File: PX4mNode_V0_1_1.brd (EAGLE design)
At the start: 48.6 x 34.9 mm, 140 parts, among them J201 DF13C-6P-1.25V, J202 DF13C-6P-1.25V, J203 DF13C-6P-1.25V, J301 DF13C-4P-1.25V, J401 DF13C-7P-1.25V, J402 DF13-4P-1.25V, J403 DF13C-4P-1.25V, J404 DF13C-4P-1.25V, J405 DF13C-4P-1.25V, J801 DF13C-3P-1.25V, M3_MOUNT1101 MOUNT-HOLE3.1MM, M3_MOUNT1102 MOUNT-HOLE3.1MM, M3_MOUNT1103 MOUNT-HOLE3.1MM, M3_MOUNT1104 MOUNT-HOLE3.1MM, U101 STM32F4X7VX, U401 MAX3051, U402 MAX3051, X101 3.2x2.5 mm / 24 MHz / 15 ppm

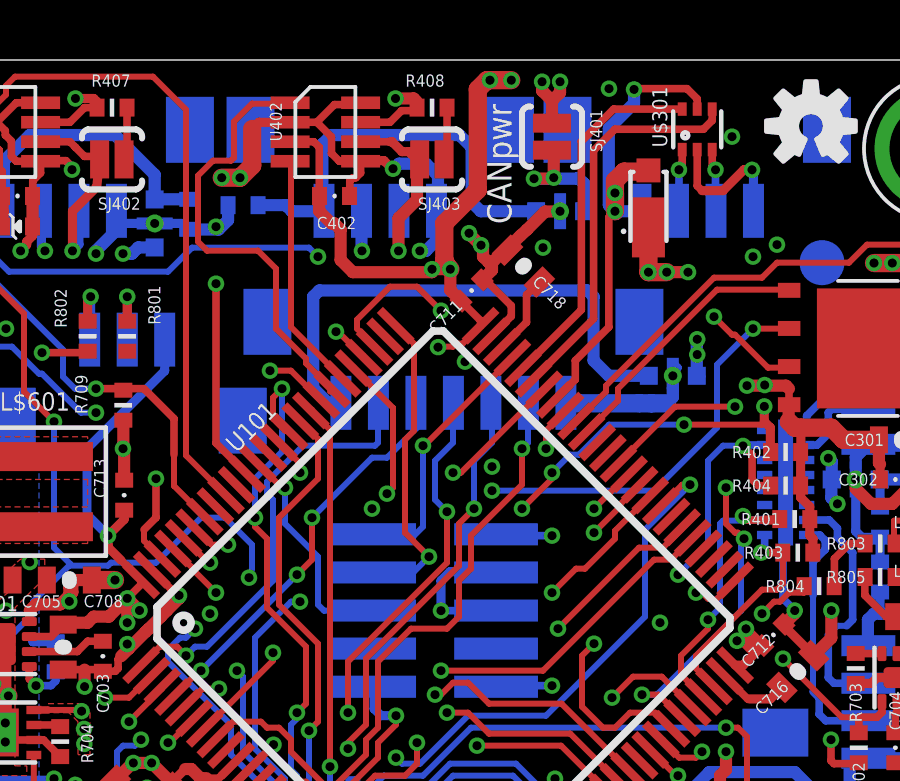
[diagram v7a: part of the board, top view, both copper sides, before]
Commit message: Cleared more clearance errors
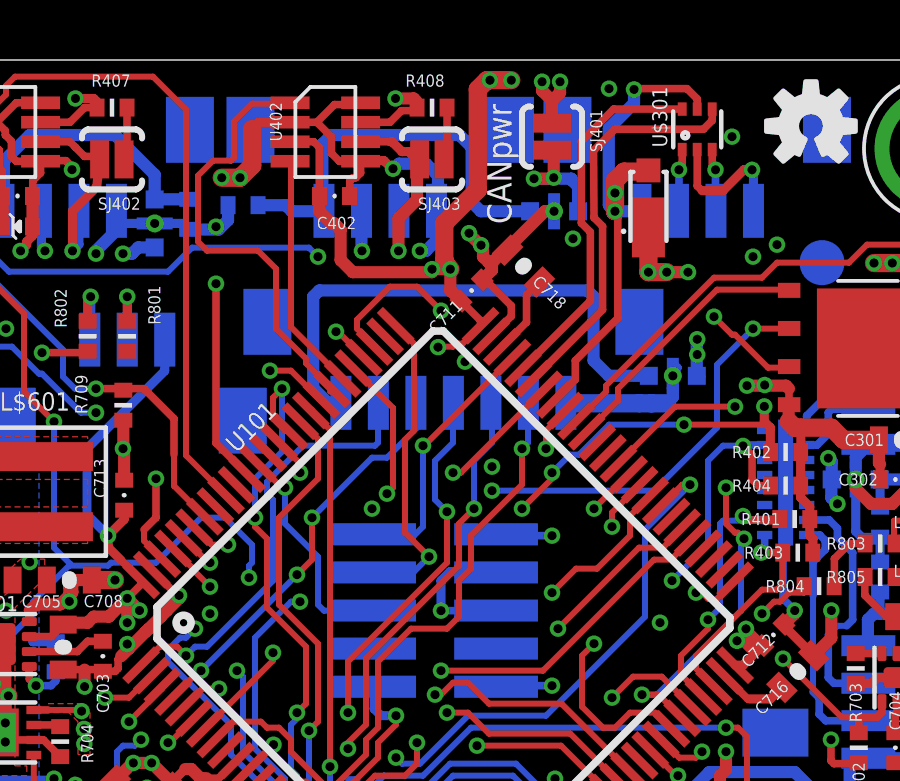
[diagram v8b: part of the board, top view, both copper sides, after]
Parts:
- moved L406 0.20 mm to (42.3, 32.6)
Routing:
- net FMU-CH3: track 44.1 -> 45.4 mm
- net GND: track 231.3 -> 230.2 mm
- net FMU-CH5: track 30.3 -> 29.4 mm
- net VDD_5V: track 80.1 -> 80.7 mm
- net FMU-UART8_RX: track 18.0 -> 17.5 mm
